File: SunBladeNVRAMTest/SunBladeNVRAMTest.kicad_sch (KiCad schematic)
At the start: 4 parts, among them U1 M48T59Y-70MH1, U2 74HC595, U3 74HC595

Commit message: a few minor corrections to the test circuit
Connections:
- net VCC: now also U2.16 (VCC), U3.16 (VCC)
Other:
- note added: "Note: this symbol is shown as the M48T59YU-70MH1, which is the surface mount variant lacking the battery and clock crystal. However, in this test circuit, it should be the full DIP module (based on the PCB designs in the SunBladeNVRAM subdirectory). Or, it could be an actual DIP-format M48T59Y (e.g., M48T59Y-70PC)."
- note removed: "Note: this symbol is shown as the M48T59YU-70MH1, which is the surface mount variant lacking the battery and clock crystal. However, in this test circuit, it should be the full DIP module (based on the PCB designs in the SunBladeNVRAM subdirectory)."
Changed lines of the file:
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@@
 	(wire
 		(pts
-			(xy 132.08 137.16) (xy 132.08 151.13)
+			(xy 132.08 137.16) (xy 132.08 146.05)
 		)
 		(stroke
@@
 		)
 	)
+	(wire
+		(pts
+			(xy 115.57 104.14) (xy 115.57 109.22)
+		)
+		(stroke
+			(width 0)
+			(type default)
+		)
+	)
 	(bus
 		(pts
@@
 	(wire
 		(pts
-			(xy 100.33 151.13) (xy 132.08 151.13)
+			(xy 100.33 146.05) (xy 132.08 146.05)
 		)
 		(stroke
@@
 		)
 	)
+	(wire
+		(pts
+			(xy 115.57 154.94) (xy 115.57 157.48)
+		)
+		(stroke
+			(width 0)
+			(type default)
+		)
+	)
 	(bus
 		(pts
@@
 	(wire
 		(pts
-			(xy 100.33 151.13) (xy 100.33 162.56)
+			(xy 100.33 146.05) (xy 100.33 162.56)
 		)
 		(stroke
@@
 		)
 	)
-	(text "Note: this symbol is shown as the\nM48T59YU-70MH1, which is the surface\nmount variant lacking the battery and\nclock crystal. However, in this test\ncircuit, it should be the full DIP\nmodule (based on the PCB designs in the\nSunBladeNVRAM subdirectory)."
+	(text "Note: this symbol is shown as the\nM48T59YU-70MH1, which is the surface\nmount variant lacking the battery and\nclock crystal. However, in this test\ncircuit, it should be the full DIP\nmodule (based on the PCB designs in the\nSunBladeNVRAM subdirectory).\n\nOr, it could be an actual DIP-format\nM48T59Y (e.g., M48T59Y-70PC)."
 		(exclude_from_sim no)
-		(at 177.546 104.394 0)
+		(at 177.038 107.188 0)
 		(effects
 			(font
@@
 	(symbol
 		(lib_id "power:VCC")
+		(at 115.57 154.94 0)
+		(unit 1)
+		(exclude_from_sim no)
+		(in_bom yes)
+		(on_board yes)
+		(dnp no)
+		(fields_autoplaced yes)
+		(property "Reference" "#PWR010"
+			(at 115.57 158.75 0)
+			(effects
+				(font
+					(size 1.27 1.27)
+				)
+				(hide yes)
+			)
+		)
+		(property "Value" "VCC"
+			(at 115.57 149.86 0)
+			(effects
+				(font
+					(size 1.27 1.27)
+				)
+			)
+		)
+		(property "Footprint" ""
+			(at 115.57 154.94 0)
+			(effects
+				(font
+					(size 1.27 1.27)
+				)
+				(hide yes)
+			)
+		)
+		(property "Datasheet" ""
+			(at 115.57 154.94 0)
+			(effects
+				(font
+					(size 1.27 1.27)
+				)
+				(hide yes)
+			)
+		)
+		(property "Description" "Power symbol creates a global label with name \"VCC\""
+			(at 115.57 154.94 0)
+			(effects
+				(font
+					(size 1.27 1.27)
+				)
+				(hide yes)
+			)
+		)
+		(pin "1"
+		)
+		(instances
+			(project ""
+				(path "/83149b9d-6d22-4817-bd95-650b7e77deef"
+					(reference "#PWR010")
+					(unit 1)
+				)
+			)
+		)
+	)
+	(symbol
+		(lib_id "power:VCC")
 		(at 87.63 165.1 0)
 		(unit 1)
@@
 					(unit 1)
 				)
+			)
+		)
+	)
+	(symbol
+		(lib_id "power:VCC")
+		(at 115.57 104.14 0)
+		(unit 1)
+		(exclude_from_sim no)
+		(in_bom yes)
+		(on_board yes)
+		(dnp no)
+		(fields_autoplaced yes)
+		(property "Reference" "#PWR09"
+			(at 115.57 107.95 0)
+			(effects
+				(font
+					(size 1.27 1.27)
+				)
+				(hide yes)
+			)
+		)
+		(property "Value" "VCC"
+			(at 115.57 99.06 0)
+			(effects
+				(font
+					(size 1.27 1.27)
+				)
+			)
+		)
+		(property "Footprint" ""
+			(at 115.57 104.14 0)
+			(effects
+				(font
+					(size 1.27 1.27)
+				)
+				(hide yes)
+			)
+		)
+		(property "Datasheet" ""
+			(at 115.57 104.14 0)
+			(effects
+				(font
+					(size 1.27 1.27)
+				)
+				(hide yes)
+			)
+		)
+		(property "Description" "Power symbol creates a global label with name \"VCC\""
+			(at 115.57 104.14 0)
+			(effects
+				(font
+					(size 1.27 1.27)
+				)
+				(hide yes)
+			)
+		)
+		(pin "1"
+		)
+		(instances
+			(project ""
+				(path "/83149b9d-6d22-4817-bd95-650b7e77deef"
+					(reference "#PWR09")
+					(unit 1)
+				)

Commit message: implement reads and writes
It turns out that not all of the pins of PORTC are
available on the Arduino Nano, so changed the test
circuit and test program to use the low 3 bits of
PORTB to interface with the high nybble of the
data bus.

I can successfully write to and read from two bytes
of memory on a DIP M48T59Y, which is good progress.
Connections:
- net D4: now also TB1.11 (D8); no longer TB1.23 (A4)
- net D5: now also TB1.12 (D9); no longer TB1.24 (A5)
- net D6: now also TB1.13 (D10); no longer TB1.25 (A6)
- net D7: now also TB1.14 (D11/MOSI); no longer TB1.26 (A7)
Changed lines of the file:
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@@
+	)
+	(junction
+		(at 118.11 21.59)
+		(diameter 0)
+		(color 0 0 0 0)
 	)
 	(junction
@@
 	)
 	(bus_entry
-		(at 21.59 63.5)
-		(size 2.54 2.54)
+		(at 115.57 81.28)
+		(size 2.54 -2.54)
+		(stroke
+			(width 0)
+			(type default)
+		)
+	)
+	(bus_entry
+		(at 115.57 76.2)
+		(size 2.54 -2.54)
 		(stroke
 			(width 0)
@@
 	)
 	(bus_entry
+		(at 115.57 78.74)
+		(size 2.54 -2.54)
+		(stroke
+			(width 0)
+			(type default)
+		)
+	)
+	(bus_entry
 		(at 143.51 73.66)
 		(size 2.54 -2.54)
@@
 	)
 	(bus_entry
-		(at 21.59 66.04)
-		(size 2.54 2.54)
-		(stroke
-			(width 0)
-			(type default)
-		)
-	)
-	(bus_entry
 		(at 246.38 73.66)
 		(size 2.54 -2.54)
@@
 	)
 	(bus_entry
-		(at 21.59 58.42)
-		(size 2.54 2.54)
+		(at 115.57 83.82)
+		(size 2.54 -2.54)
 		(stroke
 			(width 0)
@@
 		(at 140.97 119.38)
 		(size 2.54 -2.54)
-		(stroke
-			(width 0)
-			(type default)
-		)
-	)
-	(bus_entry
-		(at 21.59 60.96)
-		(size 2.54 2.54)
 		(stroke
 			(width 0)
@@
 	(wire
 		(pts
-			(xy 24.13 66.04) (xy 52.07 66.04)
+			(xy 87.63 81.28) (xy 115.57 81.28)
 		)
 		(stroke
@@
 	(bus
 		(pts
-			(xy 259.08 21.59) (xy 21.59 21.59)
+			(xy 259.08 21.59) (xy 118.11 21.59)
 		)
 		(stroke
@@
 		)
 	)
-	(wire
-		(pts
-			(xy 87.63 73.66) (xy 96.52 73.66)
+	(bus
+		(pts
+			(xy 118.11 78.74) (xy 118.11 81.28)
+		)
+		(stroke
+			(width 0)
+			(type default)
+		)
+	)
+	(wire
+		(pts
+			(xy 87.63 73.66) (xy 91.44 73.66)
 		)
 		(stroke
@@
 		)
 	)
-	(bus
-		(pts
-			(xy 21.59 60.96) (xy 21.59 63.5)
-		)
-		(stroke
-			(width 0)
-			(type default)
-		)
-	)
 	(wire
 		(pts
@@
 		)
 	)
+	(bus
+		(pts
+			(xy 118.11 73.66) (xy 118.11 76.2)
+		)
+		(stroke
+			(width 0)
+			(type default)
+		)
+	)
 	(wire
 		(pts
@@
 	(bus
 		(pts
+			(xy 118.11 76.2) (xy 118.11 78.74)
+		)
+		(stroke
+			(width 0)
+			(type default)
+		)
+	)
+	(bus
+		(pts
 			(xy 248.92 40.64) (xy 248.92 60.96)
 		)
@@
 		)
 	)
-	(wire
-		(pts
-			(xy 24.13 63.5) (xy 52.07 63.5)
+	(bus
+		(pts
+			(xy 118.11 21.59) (xy 118.11 73.66)
+		)
+		(stroke
+			(width 0)
+			(type default)
+		)
+	)
+	(wire
+		(pts
+			(xy 87.63 78.74) (xy 115.57 78.74)
 		)
 		(stroke
@@
 	(bus
 		(pts
+			(xy 118.11 21.59) (xy 21.59 21.59)
+		)
+		(stroke
+			(width 0)
+			(type default)
+		)
+	)
+	(bus
+		(pts
 			(xy 143.51 121.92) (xy 143.51 124.46)
 		)
@@
 		)
 	)
-	(bus
-		(pts
-			(xy 21.59 58.42) (xy 21.59 60.96)
-		)
-		(stroke
-			(width 0)
-			(type default)
-		)
-	)
 	(wire
 		(pts
@@
 		)
 	)
-	(bus
-		(pts
-			(xy 21.59 55.88) (xy 21.59 58.42)
-		)
-		(stroke
-			(width 0)
-			(type default)
-		)
-	)
 	(wire
 		(pts
@@
 		)
 	)
-	(bus
-		(pts
-			(xy 21.59 63.5) (xy 21.59 66.04)
-		)
-		(stroke
-			(width 0)
-			(type default)
-		)
-	)
-	(wire
-		(pts
-			(xy 24.13 68.58) (xy 52.07 68.58)
+	(wire
+		(pts
+			(xy 87.63 83.82) (xy 115.57 83.82)
 		)
 		(stroke
@@
 	(wire
 		(pts
-			(xy 24.13 60.96) (xy 52.07 60.96)
+			(xy 87.63 76.2) (xy 115.57 76.2)
 		)
 		(stroke
@@
 	)
 	(label "D4"
-		(at 26.67 60.96 0)
+		(at 110.49 76.2 0)
 		(fields_autoplaced yes)
 		(effects
@@
 	)
 	(label "D5"
-		(at 26.67 63.5 0)
+		(at 110.49 78.74 0)
 		(fields_autoplaced yes)
 		(effects
@@
 	)
 	(label "D7"
-		(at 26.67 68.58 0)
+		(at 110.49 83.82 0)
 		(fields_autoplaced yes)
 		(effects
@@
 	)
 	(label "D6"
-		(at 26.67 66.04 0)
+		(at 110.49 81.28 0)
 		(fields_autoplaced yes)
 		(effects
@@
 	(global_label "M48T59Y_NE"
 		(shape input)
-		(at 96.52 73.66 0)
+		(at 91.44 73.66 0)
 		(fields_autoplaced yes)
 		(effects
@@
 		)
 		(property "Intersheetrefs" "${INTERSHEET_REFS}"
-			(at 111.2979 73.66 0)
+			(at 106.2179 73.66 0)
 			(effects
 				(font

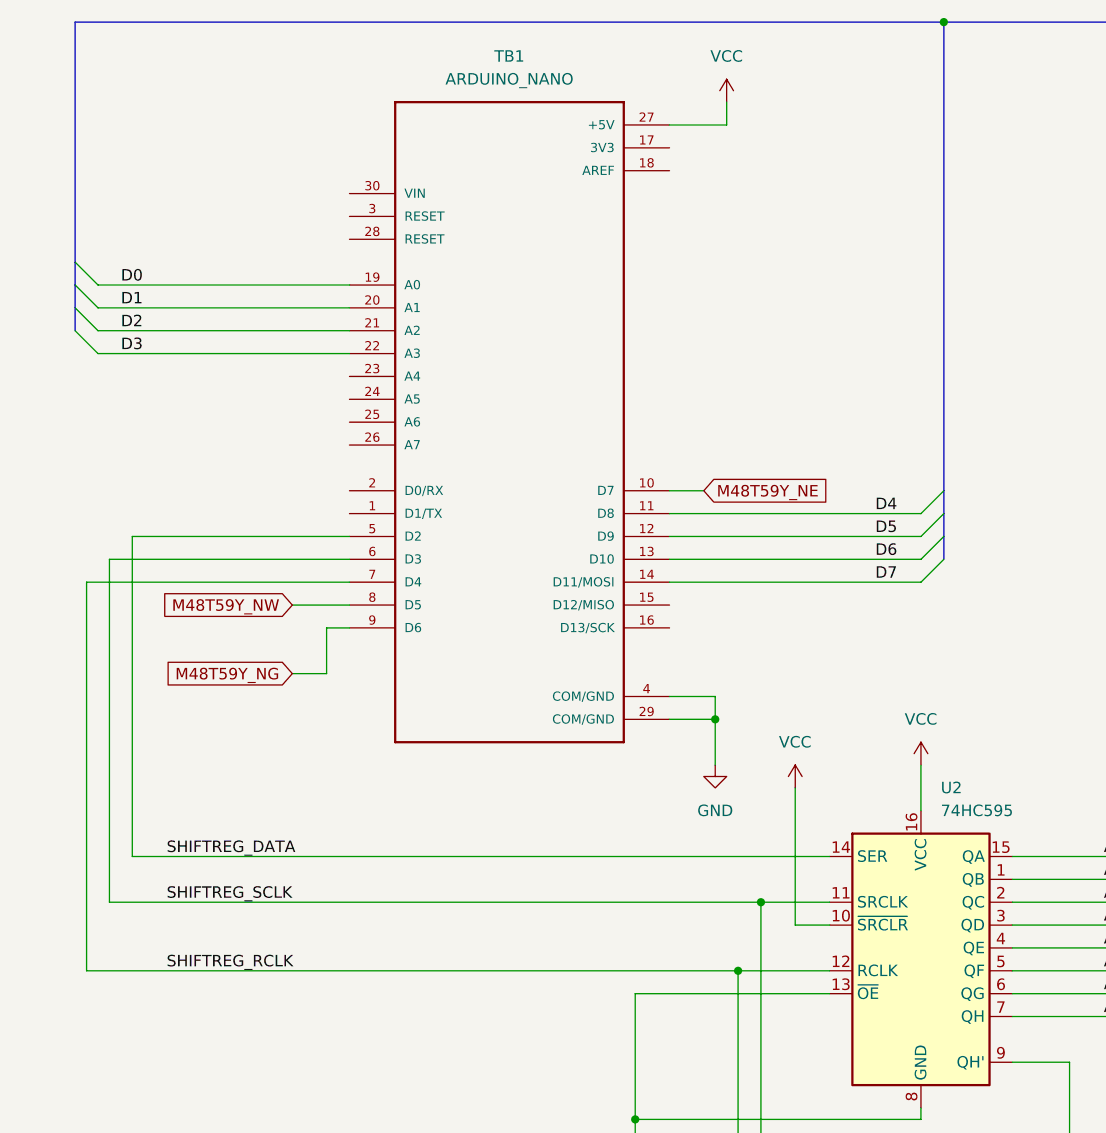
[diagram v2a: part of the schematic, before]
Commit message: add pull-ups to -E, -G, and -W signals
The idea is to try to avoid any spurious writes to
the M48T59Y on power-up or reset.
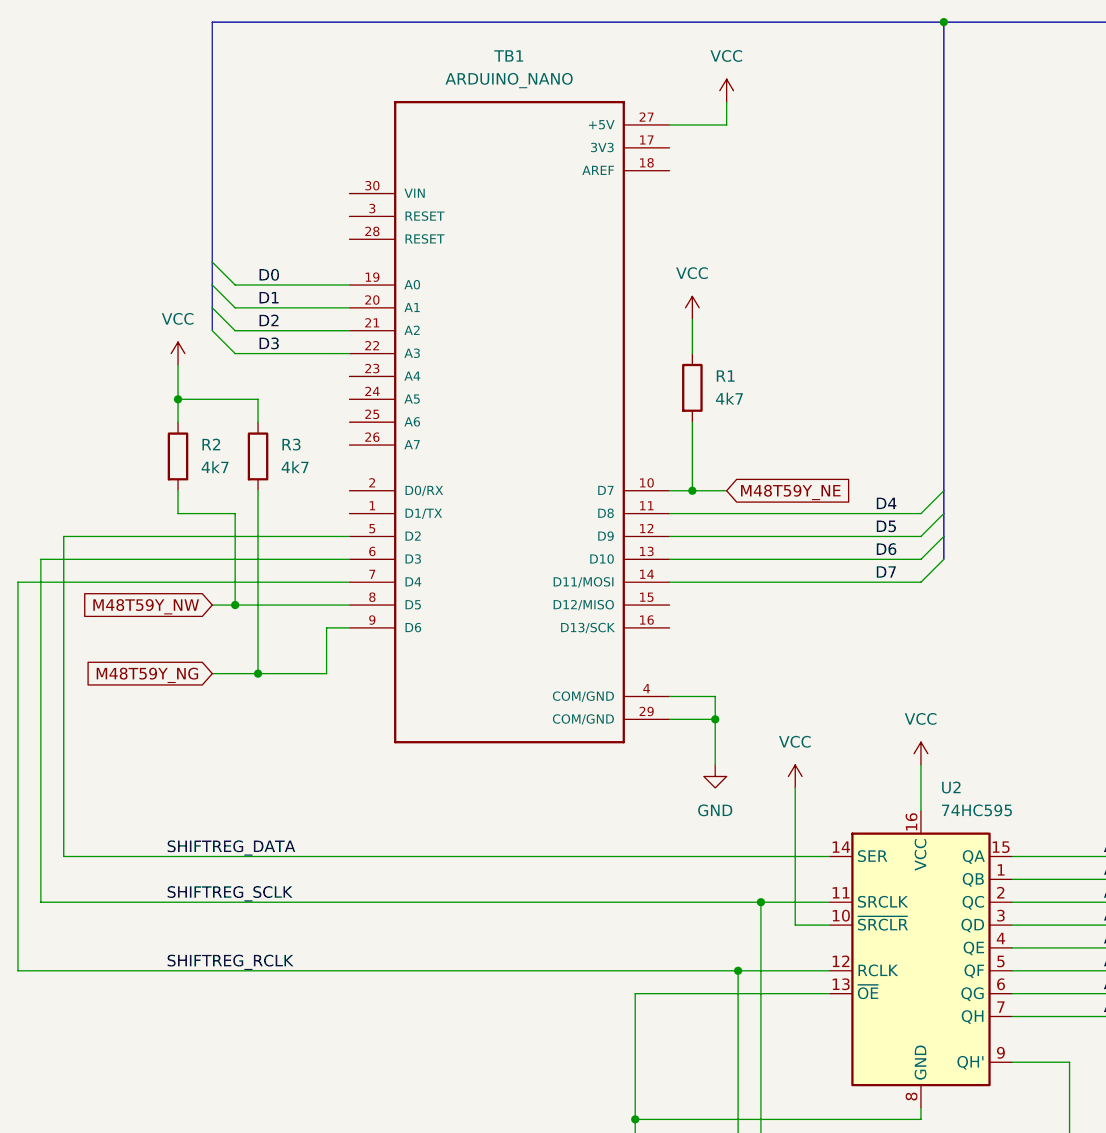
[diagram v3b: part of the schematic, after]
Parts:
- added R1, R2, R3: 4k7, symbol Device:R
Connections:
- net M48T59Y_NE: now also R1.2
- net M48T59Y_NG: now also R3.2
- net M48T59Y_NW: now also R2.2
- net VCC: now also R1.1, R2.1, R3.1

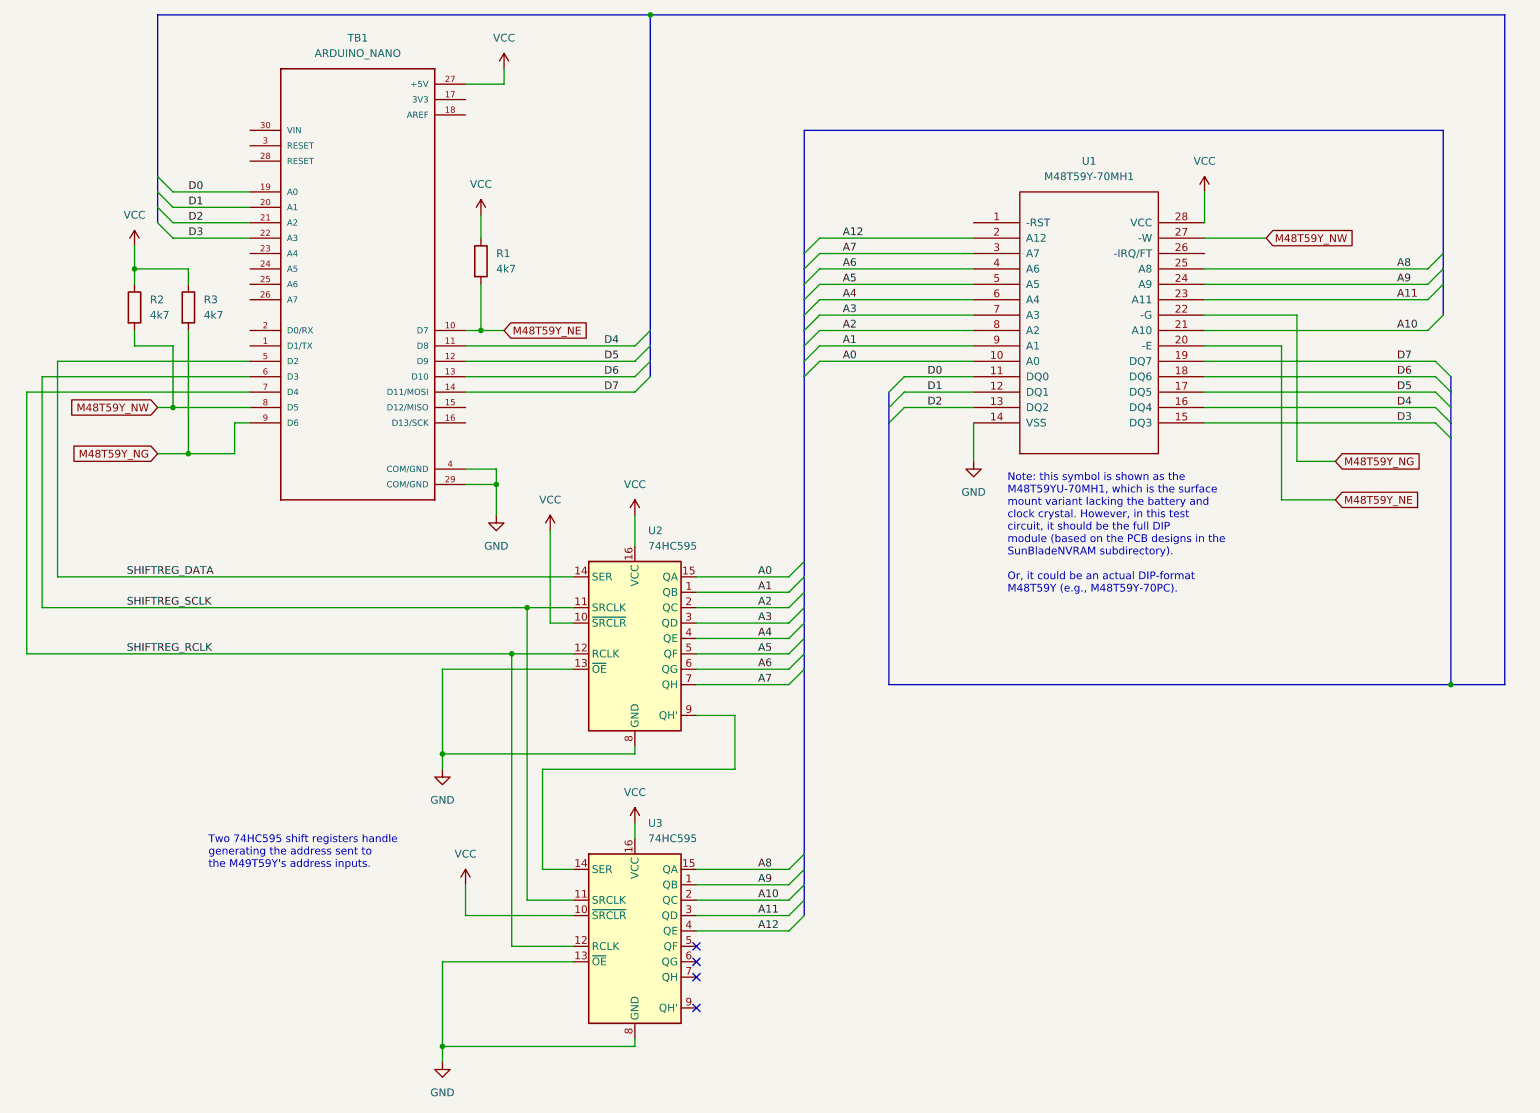
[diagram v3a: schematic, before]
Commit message: add GO and LOG pushbuttons
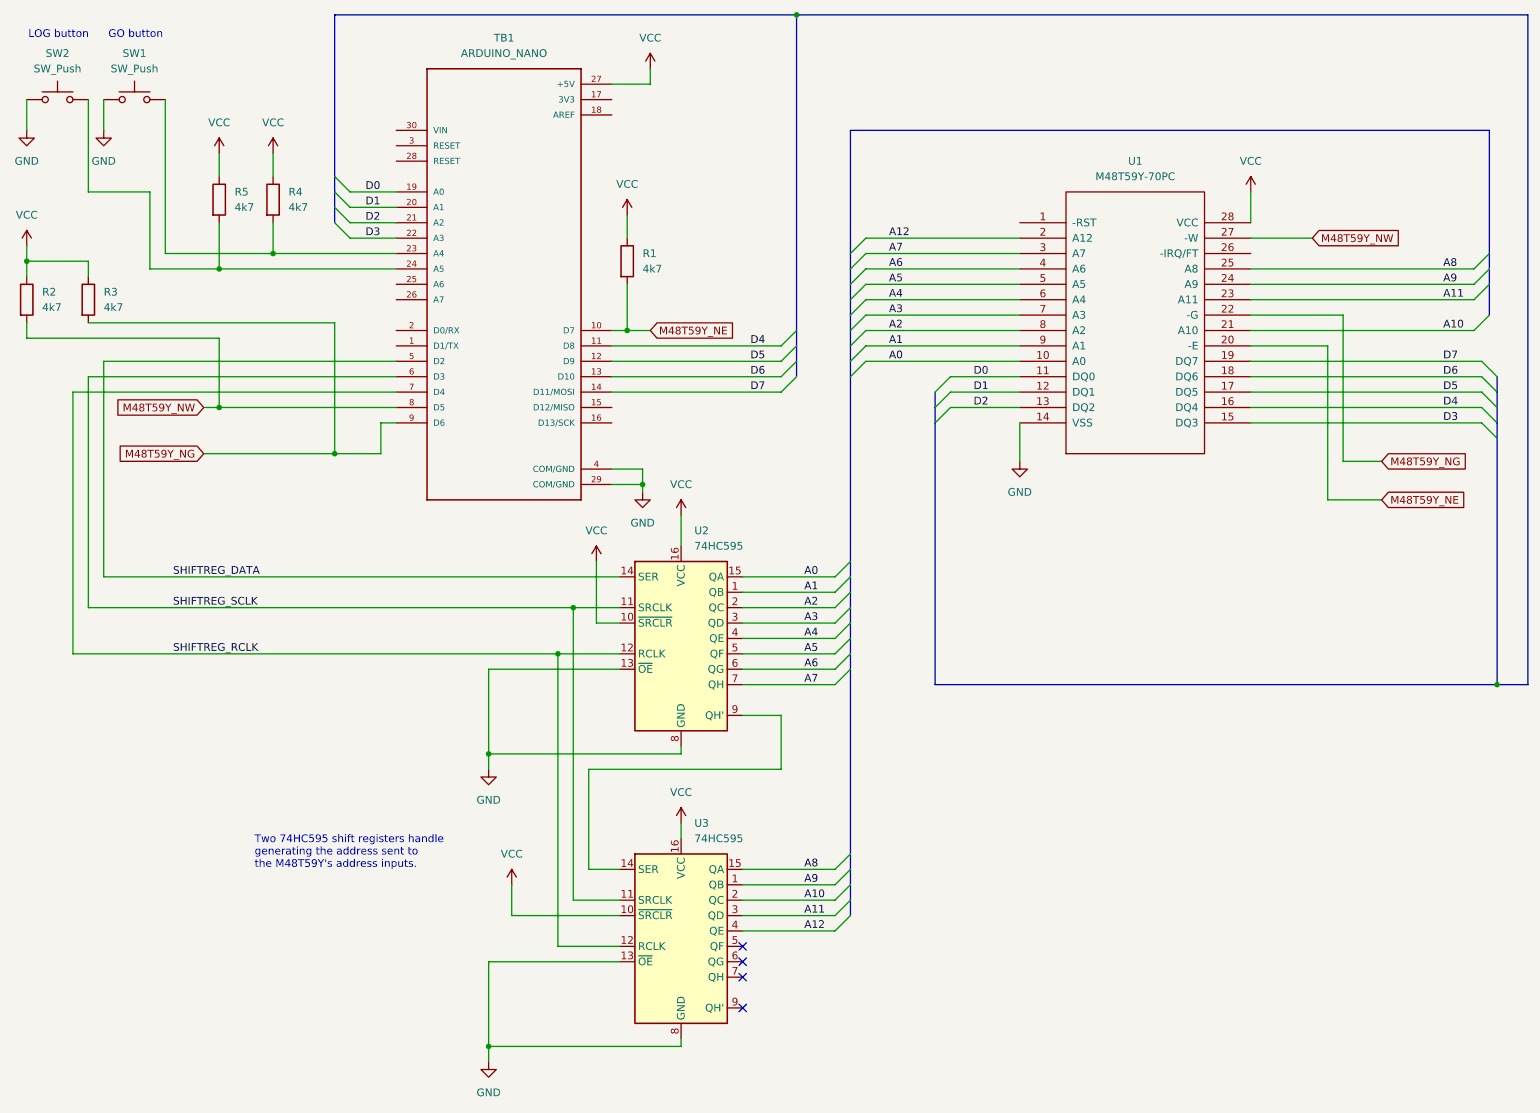
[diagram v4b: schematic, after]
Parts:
- added R4, R5: 4k7, symbol Device:R
- added SW1, SW2: SW_Push, symbol Switch:SW_Push
- U1: value M48T59Y-70MH1 -> M48T59Y-70PC
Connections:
- net GND: now also SW1.1, SW2.1
- net VCC: now also R4.1, R5.1
- net at TB1.23 (A4): now also R4.2, SW1.2
- net at TB1.24 (A5): now also R5.2, SW2.2
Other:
- note added: "GO button"
- note added: "LOG button"
- note added: "Two 74HC595 shift registers handle generating the address sent to the M48T59Y's address inputs."
- note removed: "Note: this symbol is shown as the M48T59YU-70MH1, which is the surface mount variant lacking the battery and clock crystal. However, in this test circuit, it should be the full DIP module (based on the PCB designs in the SunBladeNVRAM subdirectory). Or, it could be an actual DIP-format M48T59Y (e.g., M48T59Y-70PC)."
- note removed: "Two 74HC595 shift registers handle generating the address sent to the M49T59Y's address inputs."
- moved on the sheet: R1, R2, R3, TB1, U1, U2, U3
